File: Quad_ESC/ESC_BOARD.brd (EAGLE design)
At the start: 139.7 x 40.6 mm, 32 parts, among them U1 SN74CBTLV3257PWR, Y1 ECS-80-S-4X

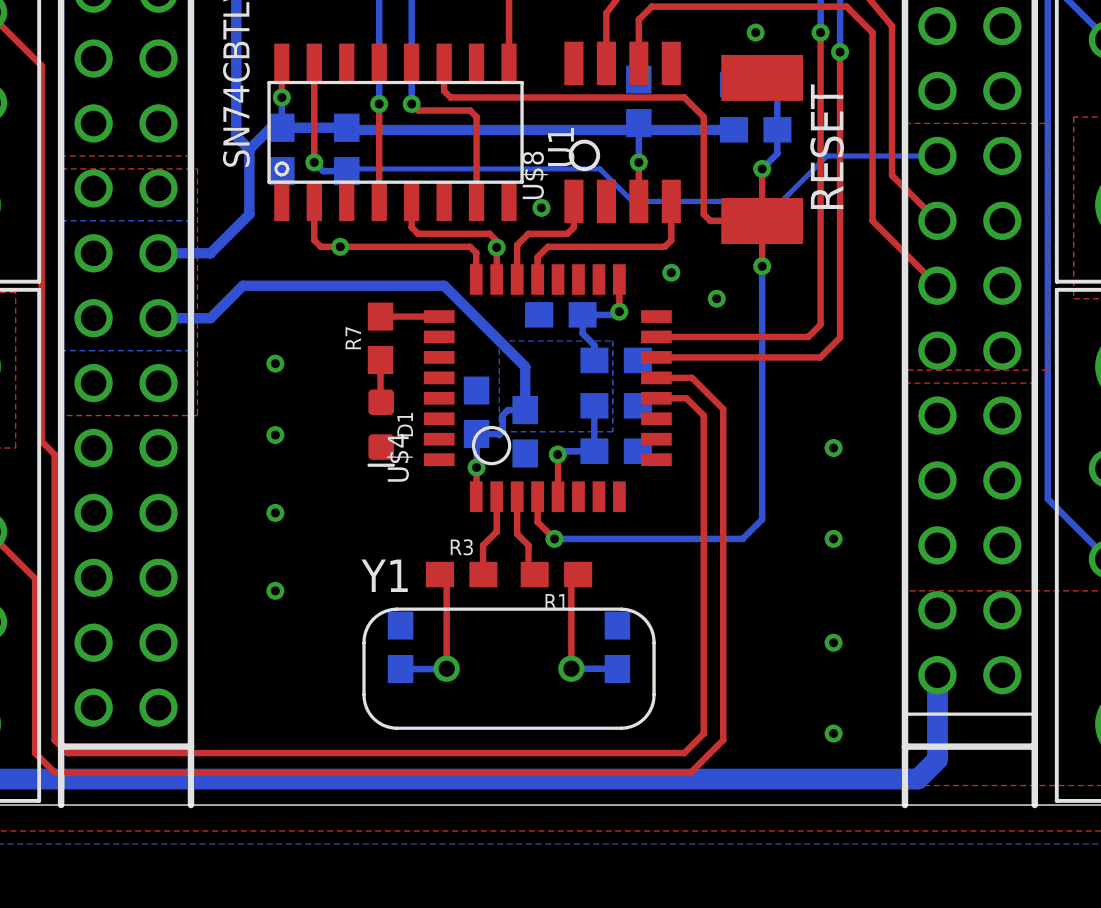
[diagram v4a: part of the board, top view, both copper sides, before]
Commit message: cad for connectors to backplane
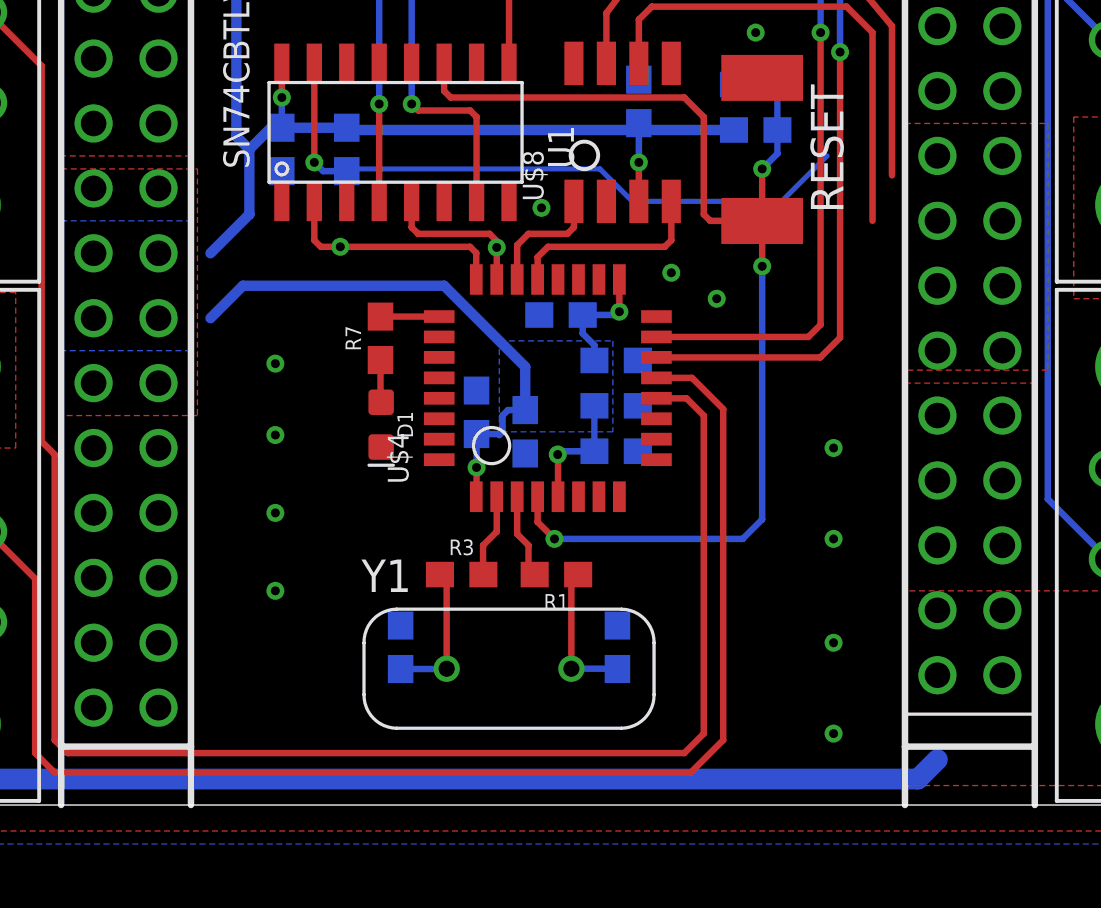
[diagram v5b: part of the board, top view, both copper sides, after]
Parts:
- U$1: device ESC_to_Backplane_Connectors:ESC2BACKPLANE_WHOLE -> ESC_to_Backplane_Connectors_esc:ESC2BACKPLANE_WHOLE
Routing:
- net PROG_SEL: track 29.7 -> 25.4 mm
- net +3V3: track 75.0 -> 70.9 mm
- net CAN_L: track 22.4 -> 18.9 mm
- net +12V: track 66.3 -> 62.9 mm
- net CAN_H: track 22.7 -> 20.2 mm

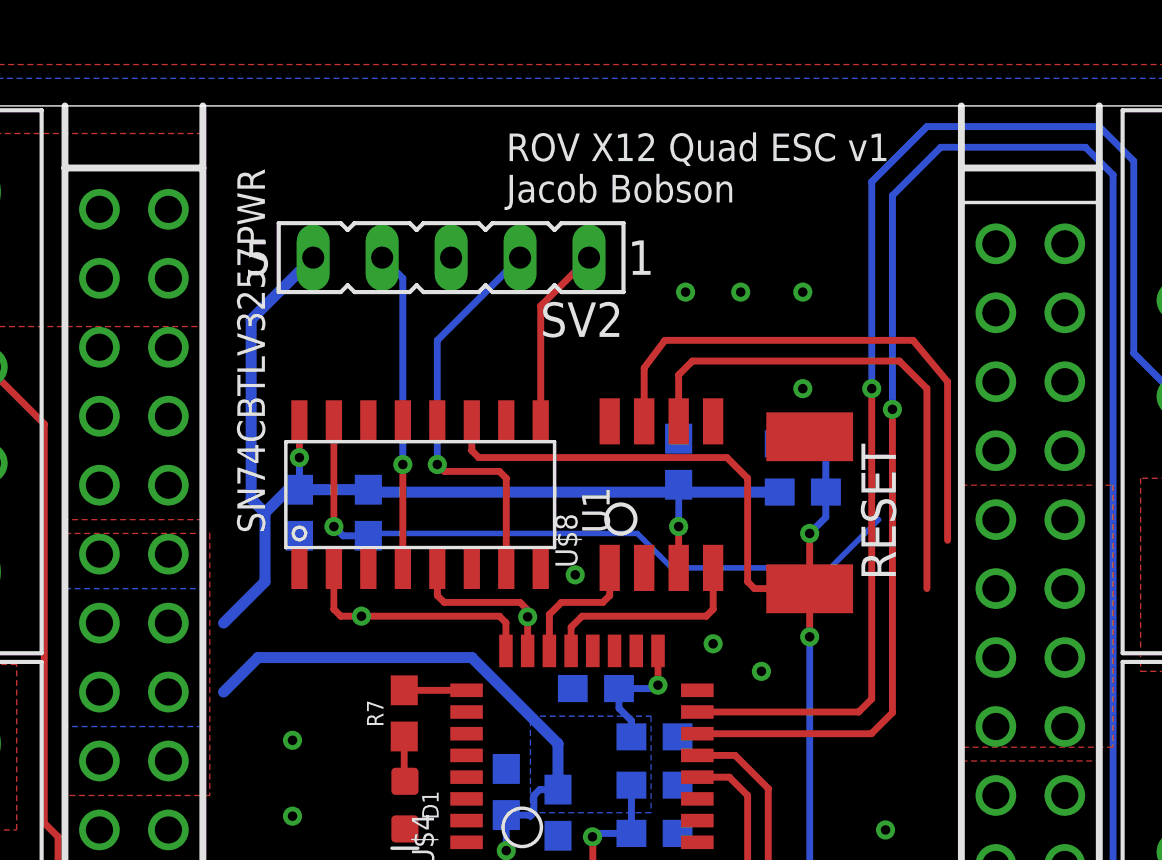
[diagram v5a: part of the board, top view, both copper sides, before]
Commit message: fix routings undone by connector switch for cad
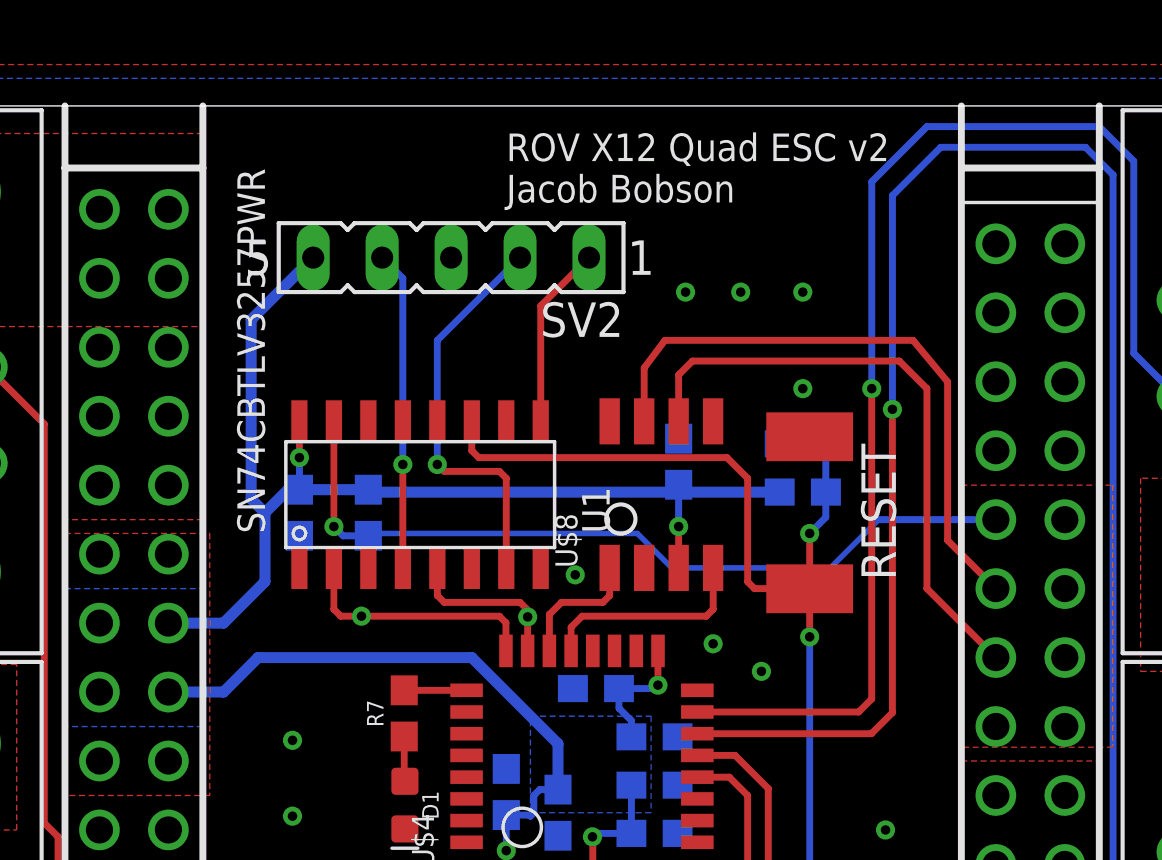
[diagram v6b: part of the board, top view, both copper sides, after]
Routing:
- net PROG_SEL: track 25.4 -> 29.7 mm
- net +3V3: track 70.9 -> 75.0 mm
- net CAN_L: track 18.9 -> 22.4 mm
- net CAN_H: track 20.2 -> 22.7 mm
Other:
- board text added: "ROV X12 Quad ESC v2 Jacob Bobson"
- board text removed: "ROV X12 Quad ESC v1 Jacob Bobson"
